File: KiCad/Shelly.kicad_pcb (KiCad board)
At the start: 2 copper layers, 16 x 31 mm, 12 parts, among them J1 USB-C, J2 Shelly i3, J3 Shelly 1, J4 Shelly 2, M1 D24V5F3-NoSHDN, SW1 GPIO0, U1 FT230XQ

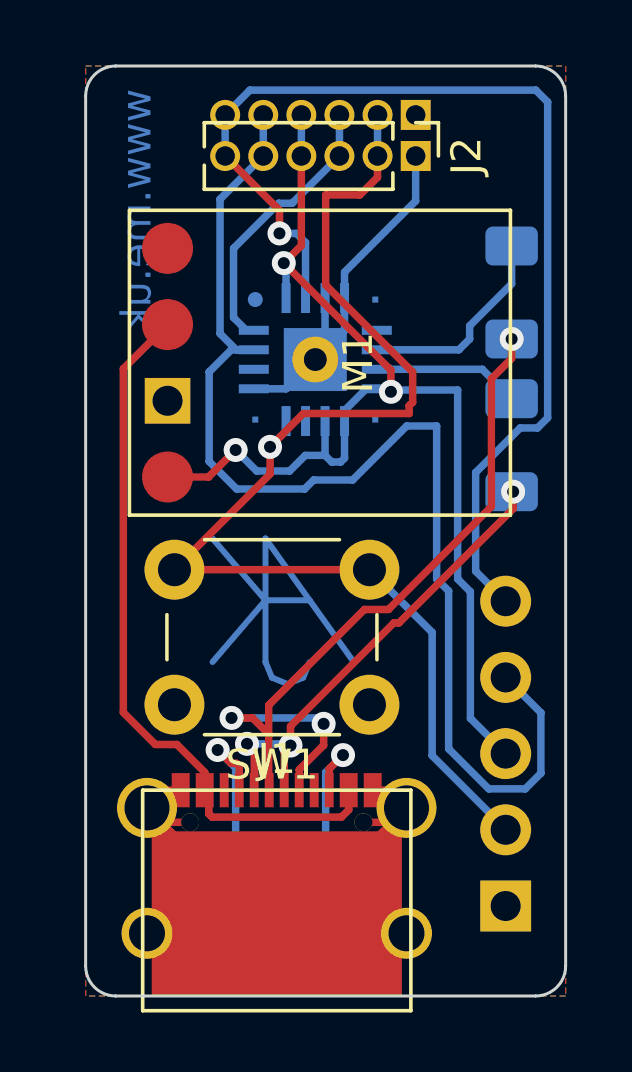
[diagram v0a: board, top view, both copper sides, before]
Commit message: Swapped around for easier soldering with heat gun
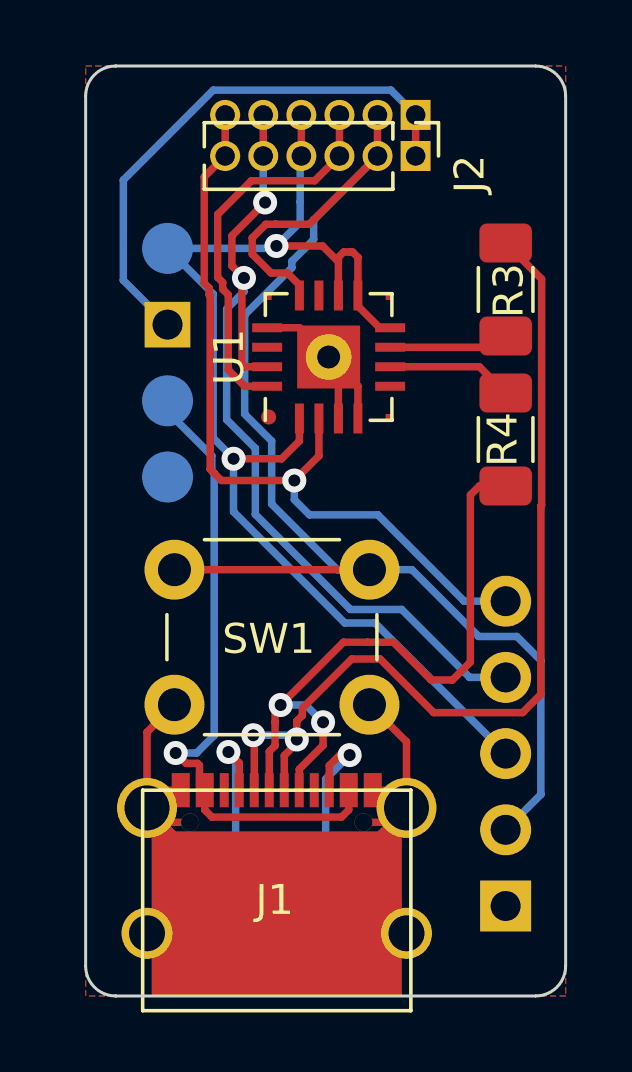
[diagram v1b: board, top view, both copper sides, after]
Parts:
- removed AJK1: AJK, RevK:AJK
- M1: moved to B.Cu
- R3, R4, U1: moved to F.Cu
- moved R3 5.19 mm to (184.0, 66.5), turned to 270 degrees
- moved R4 4.90 mm to (184.0, 71.5)
- moved U1 0.45 mm to (178.1, 68.7), turned to 90 degrees
- turned M1 to 90 degrees
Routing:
- net GND: track 39.6 -> 60.1 mm
- net Net-(J1-PadA7): track 16.3 -> 31.5 mm, vias 3 -> 2
- net RXD: track 41.3 -> 29.0 mm, vias 0 -> 2
- net TXD: track 37.2 -> 26.6 mm
- net GPIO0: track 41.2 -> 47.1 mm, vias 1 -> 0
- net Net-(J1-PadA6): track 26.0 -> 22.1 mm, vias 3 -> 2
- net RST: track 9.33 -> 13.1 mm
- net D+: track 6.92 -> 4.21 mm
- net VBUS: track 24.0 -> 21.5 mm, vias 0 -> 1
- net +3V3: track 38.7 -> 41.0 mm, vias 3 -> 2
- net D-: track 4.90 -> 4.01 mm
- net Net-(J1-PadA5): track 5.60 -> 5.06 mm
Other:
- board text removed: "www.me.uk"

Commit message: V2 Shelly using FT231XQ
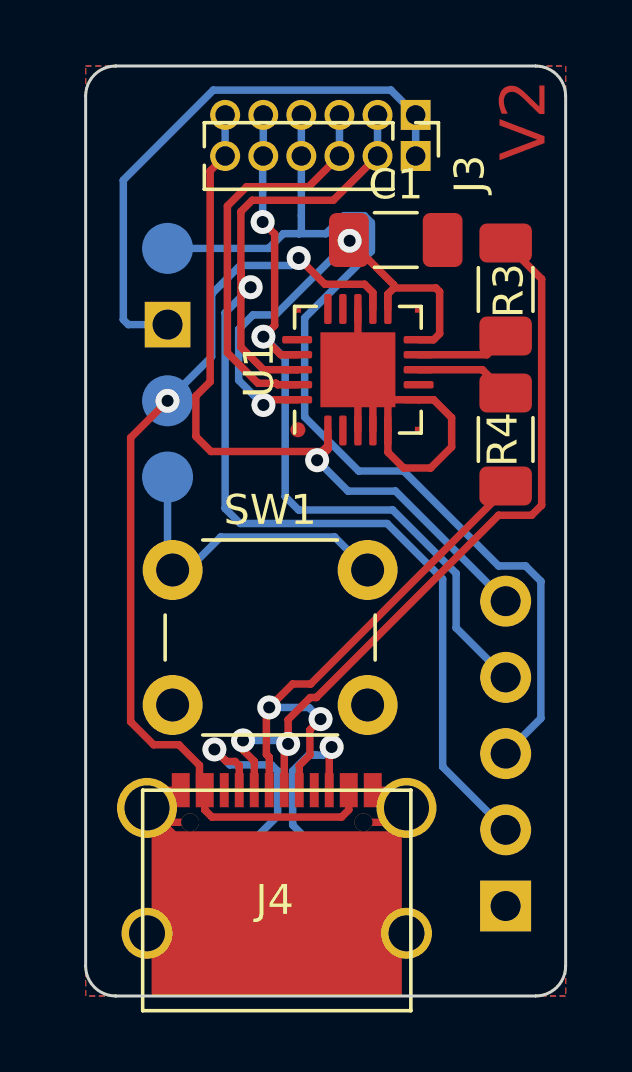
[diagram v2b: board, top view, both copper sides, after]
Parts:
- added C1: 100nF, Capacitor_SMD:C_1206_3216Metric_Pad1.33x1.80mm_HandSolder, F.Cu at (180.3, 64.8)
- SW1: value GPIO0 -> SW_Push
- U1: value FT230XQ -> FT231XQ; footprint RevK:QFN-16-(hand)-1EP_4x4mm_P0.65mm_EP2.1x2.1mm -> RevK:QFN-20-(hand)-1EP_4x4mm_P0.5mm_EP2.5x2.5mm
- moved SW1 7.95 mm to (172.9, 75.8), turned to 0 degrees
- moved U1 1.06 mm to (179.1, 69.1)
- renumbered J3 to J1, J4 to J2, J2 to J3, J1 to J4
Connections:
- M1 pad 1: Net-(M1-Pad1) -> SHDN
- SW1 pad 1: GND -> SHDN
- SW1 pad 2: GPIO0 -> GND
- U1 pad 1: +3V3 -> TXD
- U1 pad 10: +3V3 -> Net-(C1-Pad1)
- U1 pad 11: Net-(U1-Pad11) -> Net-(C1-Pad1)
- U1 pad 12: GPIO0 -> VBUS
- U1 pad 15: RXD -> Net-(U1-Pad15)
- U1 pad 16: RST -> Net-(U1-Pad16)
- U1 pad 17: GND -> RXD
- U1 pad 2: TXD -> Net-(U1-Pad2)
- U1 pad 5: Net-(U1-Pad5) -> GND
- U1 pad 6: D+ -> GND
- U1 pad 7: D- -> Net-(U1-Pad7)
- U1 pad 8: +3V3 -> D+
- U1 pad 9: +3V3 -> D-
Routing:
- net Net-(C1-Pad1): track 0.00 -> 15.7 mm, vias 0 -> 2
- net VBUS: track 21.5 -> 32.5 mm, vias 1 -> 2
- net SHDN: track 0.00 -> 10.6 mm
- net GPIO0: track 47.1 -> 39.2 mm, vias 0 -> 1
- net +3V3: track 41.0 -> 35.1 mm, vias 2 -> 0
- net Net-(J4-PadA7): track 31.5 -> 26.4 mm
- net GND: track 60.1 -> 55.3 mm
- net Net-(J4-PadA6): track 22.1 -> 18.4 mm
- net RXD: track 29.0 -> 25.7 mm
- net Net-(J4-PadA5): track 5.06 -> 7.76 mm
- net TXD: track 26.6 -> 25.2 mm
- net Net-(J4-PadB5): track 5.41 -> 6.46 mm
- net D+: track 4.21 -> 3.22 mm
- net D-: track 4.01 -> 3.16 mm
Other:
- board text added: "V2"

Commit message: Revised with LED
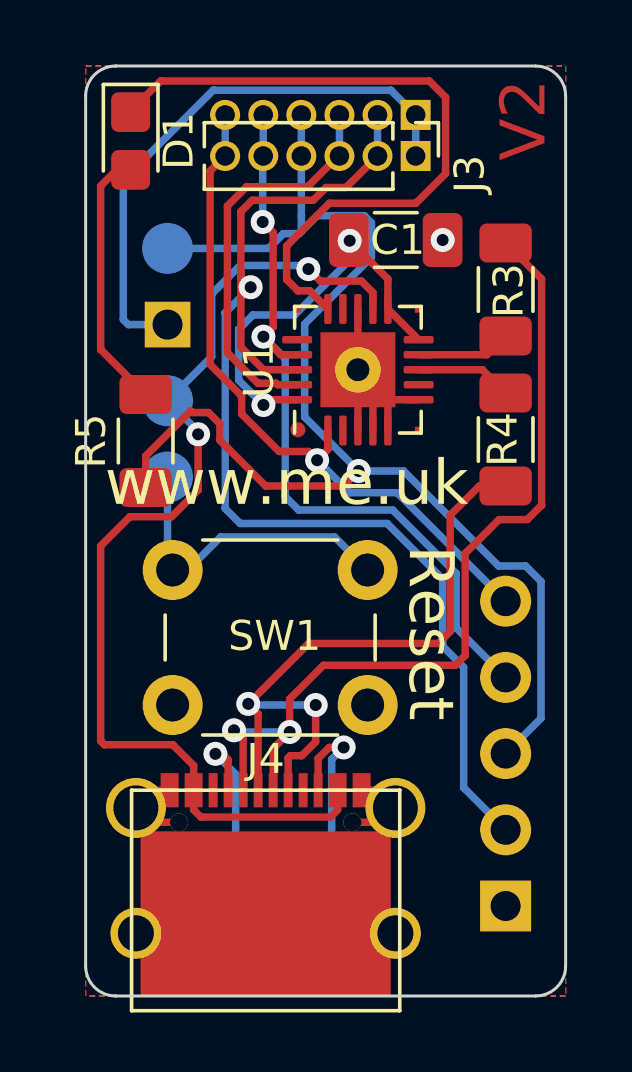
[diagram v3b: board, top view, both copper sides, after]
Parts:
- added D1: LED, LED_SMD:LED_0805_2012Metric_Castellated, F.Cu at (171.5, 61.5)
- added R5: 680R, Resistor_SMD:R_1206_3216Metric_Pad1.30x1.75mm_HandSolder, F.Cu at (172.0, 71.5)
- SW1: value SW_Push -> Reset
- moved J4 0.37 mm to (176.0, 90.0)
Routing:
- net Net-(D1-Pad1): track 0.00 -> 22.9 mm
- net GND: track 55.3 -> 39.2 mm, vias 0 -> 1
- net +3V3: track 35.1 -> 45.4 mm, vias 0 -> 1
- net Net-(D1-Pad2): track 0.00 -> 8.79 mm
- net Net-(J4-PadA6): track 18.4 -> 22.6 mm
- net Net-(J4-PadA7): track 26.4 -> 29.6 mm
- net VBUS: track 32.5 -> 35.3 mm
- net Net-(J4-PadA5): track 7.76 -> 5.27 mm
- net Net-(C1-Pad1): track 15.7 -> 13.6 mm
- net TXD: track 25.2 -> 23.1 mm
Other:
- board text added: "Reset"
- board text added: "www.me.uk"

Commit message: RST power control
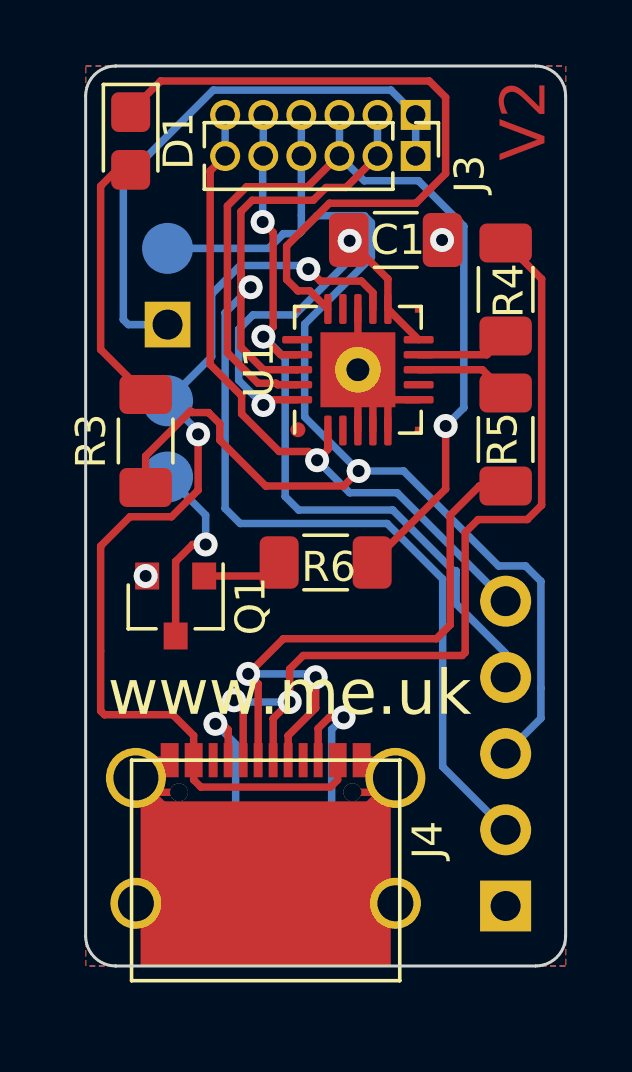
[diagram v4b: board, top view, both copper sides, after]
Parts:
- removed SW1: Reset, Button_Switch_THT:SW_PUSH_6mm
- added Q1: BC817, Package_TO_SOT_SMD:SOT-23, F.Cu at (173.0, 77.0)
- added R6: 1k, Resistor_SMD:R_1206_3216Metric_Pad1.30x1.75mm_HandSolder, F.Cu at (178.0, 75.5)
- moved J4 1.00 mm to (176.0, 89.0)
- moved R1 1.00 mm to (175.0, 86.0)
- moved R2 1.00 mm to (178.0, 86.0)
- renumbered R5 to R3, R3 to R4, R4 to R5
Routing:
- net RST: track 13.5 -> 31.0 mm, vias 0 -> 1
- net GND: track 39.2 -> 50.8 mm, vias 1 -> 2
- net SHDN: track 10.6 -> 6.50 mm, vias 0 -> 1
- net Net-(Q1-Pad1): track 0.00 -> 2.69 mm
- net VBUS: track 35.3 -> 34.3 mm
- net Net-(J4-PadA6): track 22.6 -> 21.8 mm
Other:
- board size 16 x 31 mm -> 16 x 30 mm
- board text removed: "Reset"

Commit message: Opto isolator
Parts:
- removed Q1: BC817, Package_TO_SOT_SMD:SOT-23
- added U2: TLP3546, Package_DIP:DIP-6_W7.62mm, F.Cu at (172.0, 75.2)
- R6: moved to B.Cu
- moved R6 2.28 mm to (175.8, 75.2)
- moved R3 1.54 mm to (173.2, 72.4), turned to 0 degrees
- moved R2 0.40 mm to (177.6, 86.0)
- moved R1 0.20 mm to (174.8, 86.0)
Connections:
- J1 pad 3: +3V3 -> Net-(J1-Pad3)
- M1 pad 1: SHDN -> Net-(M1-Pad1)
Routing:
- net GND: track 50.8 -> 79.7 mm, vias 2 -> 1
- net +3V3: track 45.4 -> 29.6 mm, vias 1 -> 2
- net SHDN: track 6.50 -> 0.00 mm, vias 1 -> 0
- net Net-(D1-Pad2): track 8.79 -> 13.9 mm
- net Net-(J1-Pad3): track 0.00 -> 5.06 mm
- net VBUS: track 34.3 -> 31.5 mm
- net RST: track 31.0 -> 33.9 mm, vias 1 -> 2
- net Net-(J4-PadA7): track 29.5 -> 27.6 mm
- net Net-(J4-PadA5): track 5.27 -> 6.72 mm
- net Net-(J4-PadA6): track 21.8 -> 20.6 mm
- net TXD: track 23.1 -> 24.2 mm
- net Net-(J4-PadB5): track 5.99 -> 6.75 mm
- net GPIO0: track 39.2 -> 40.0 mm
- net RXD: track 25.7 -> 26.2 mm

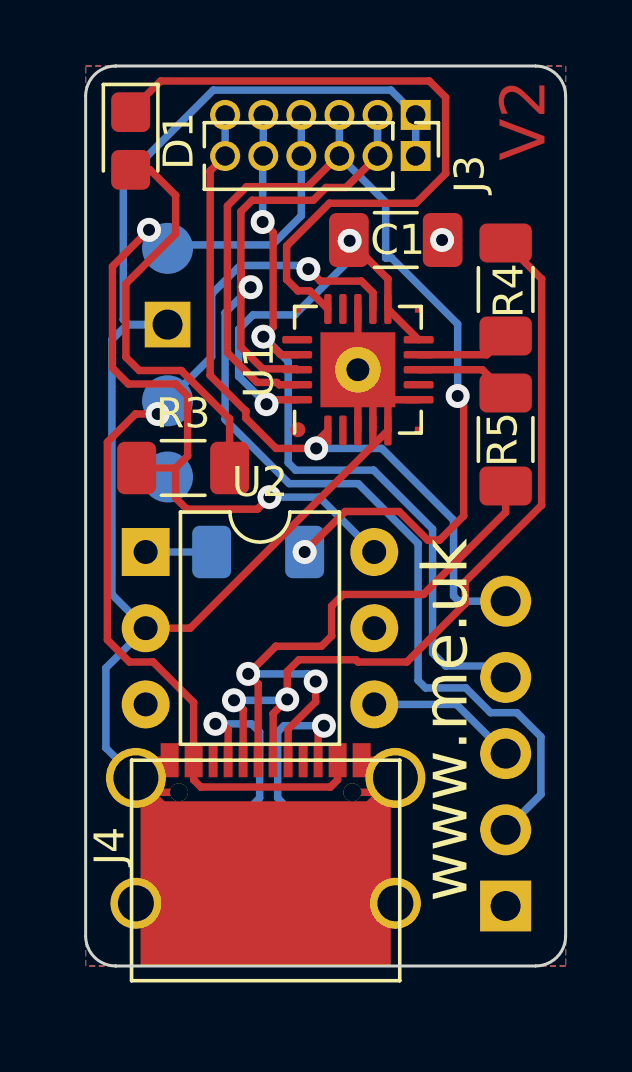
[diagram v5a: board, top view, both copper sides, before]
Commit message: Tweak tracking slightly
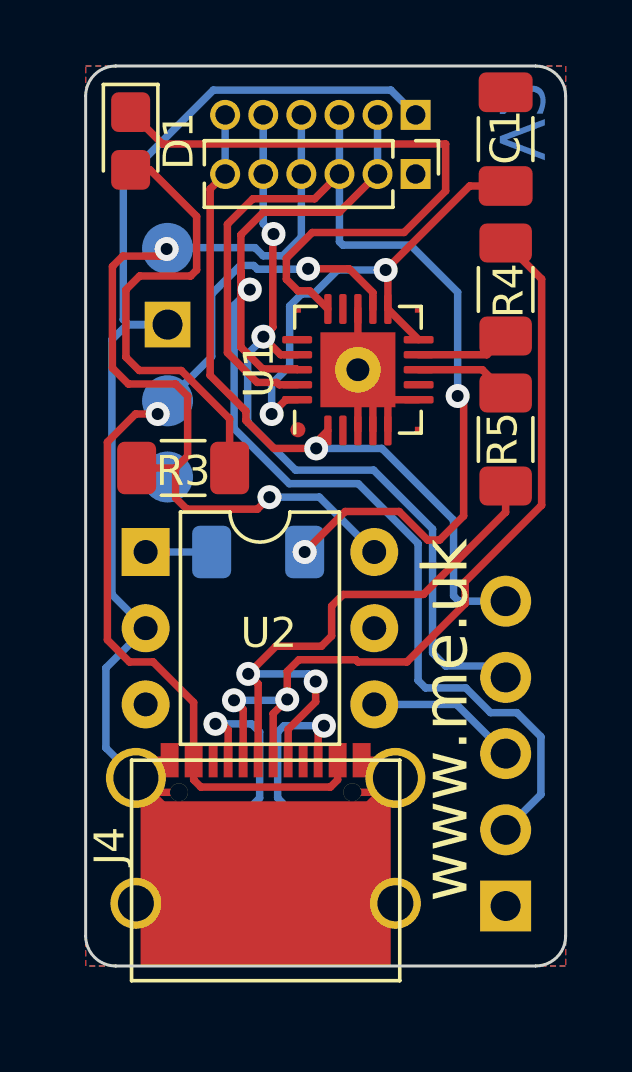
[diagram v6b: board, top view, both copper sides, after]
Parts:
- moved C1 4.97 mm to (184.0, 61.4), turned to 90 degrees
- moved J3 0.60 mm to (181.0, 62.6)
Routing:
- net GND: track 79.7 -> 67.5 mm, vias 1 -> 0
- net Net-(C1-Pad1): track 13.5 -> 16.5 mm
- net Net-(D1-Pad1): track 22.9 -> 21.2 mm
- net Net-(D1-Pad2): track 13.9 -> 15.5 mm
- net RST: track 33.9 -> 34.5 mm

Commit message: FT231XQ
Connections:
- U1 pad 2: Net-(U1-Pad2) -> GND
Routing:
- net GND: track 67.5 -> 69.8 mm

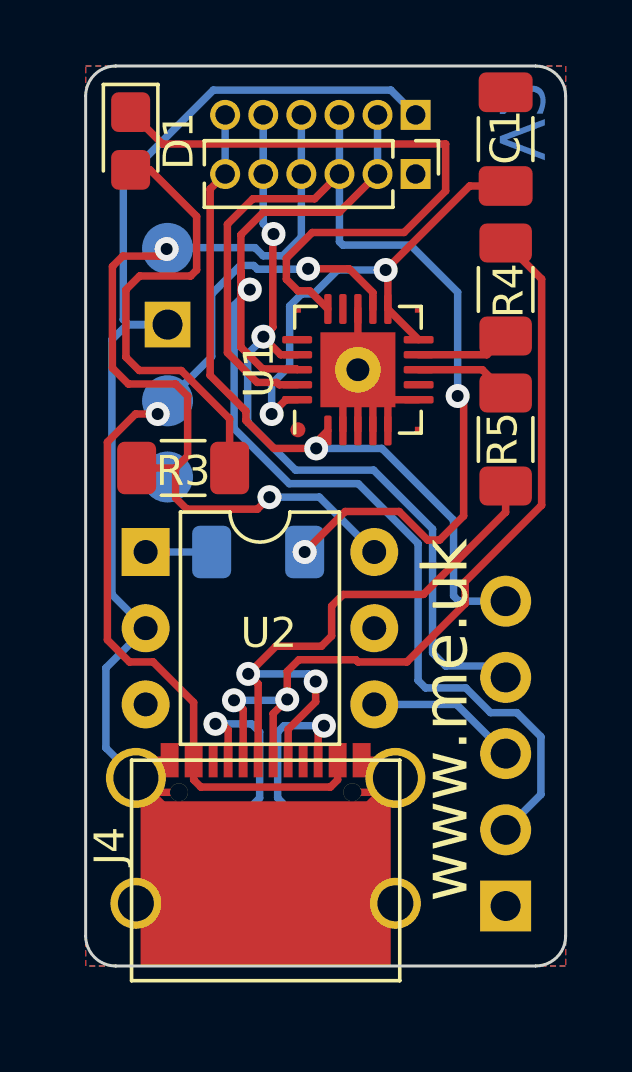
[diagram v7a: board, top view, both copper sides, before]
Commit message: Fix VBUS via
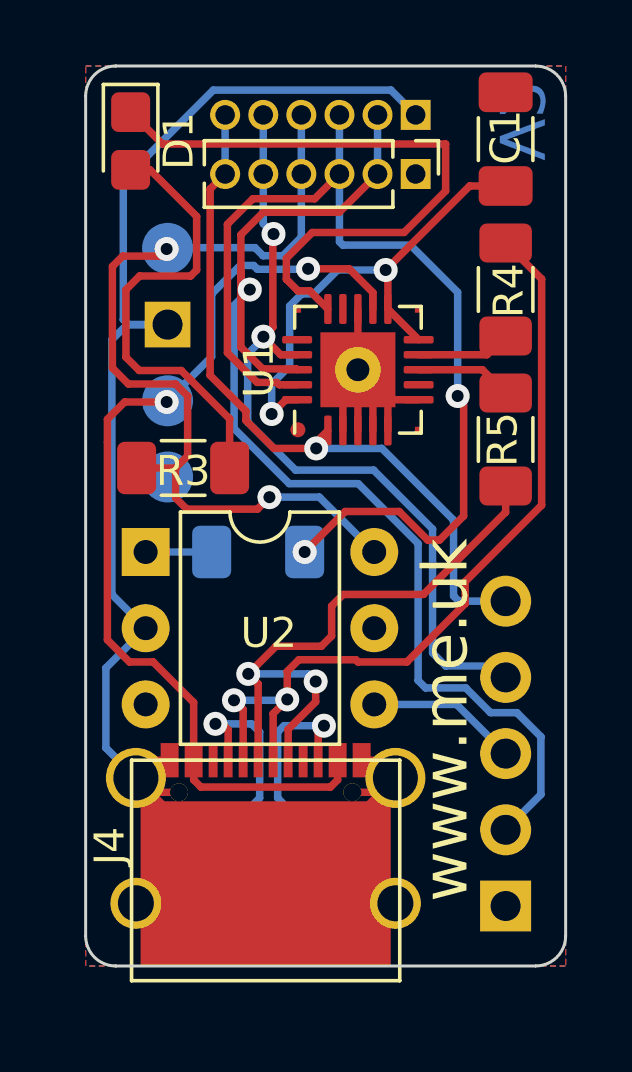
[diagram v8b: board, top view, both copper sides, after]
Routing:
- net VBUS: track 31.5 -> 32.4 mm
